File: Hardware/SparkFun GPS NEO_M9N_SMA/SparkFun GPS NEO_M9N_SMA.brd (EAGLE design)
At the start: 40.6 x 33 mm, 89 parts, among them J2 Qwiic Right Angle, J4 Qwiic Right Angle, U1 U-BLOX_NEO-M9N, U2 3.3V, Y1 GPS_CHIP_ANTENNAW3011

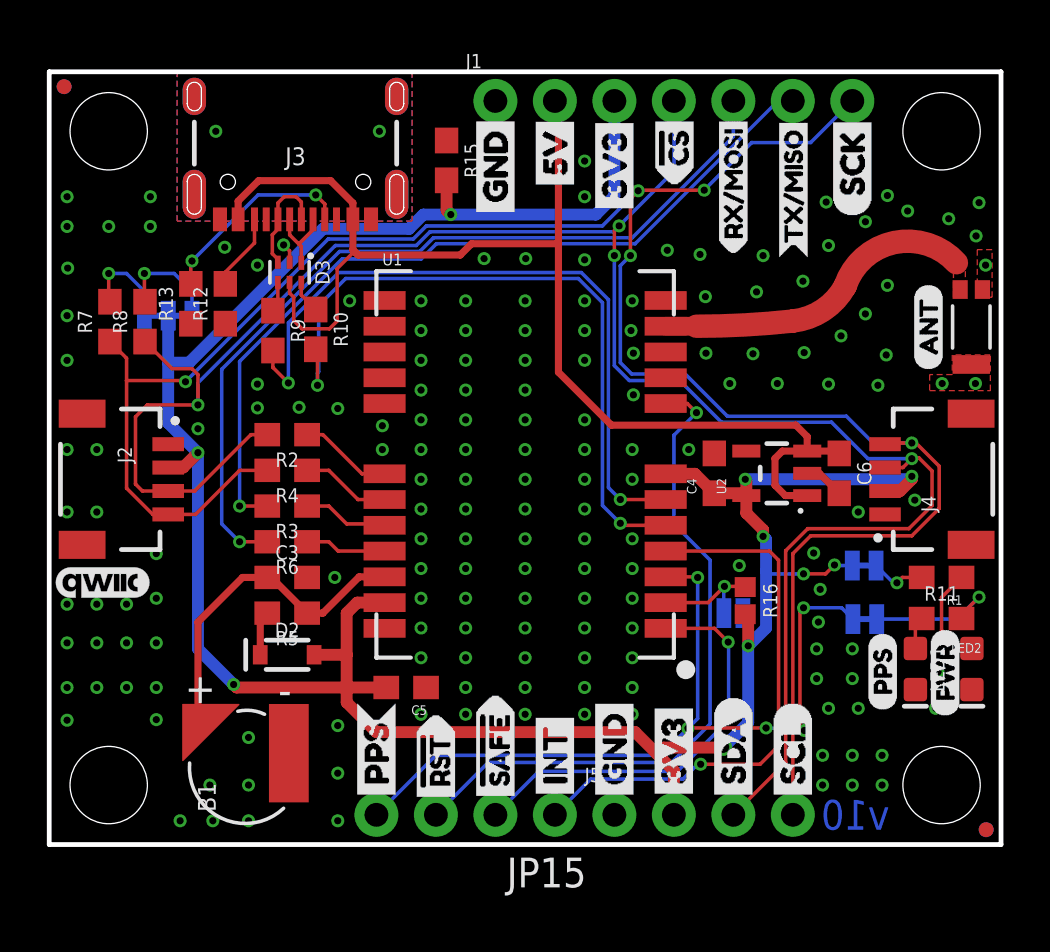
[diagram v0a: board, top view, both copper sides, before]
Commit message: Restore chip antenna version, and moves SMA version to its' own folder
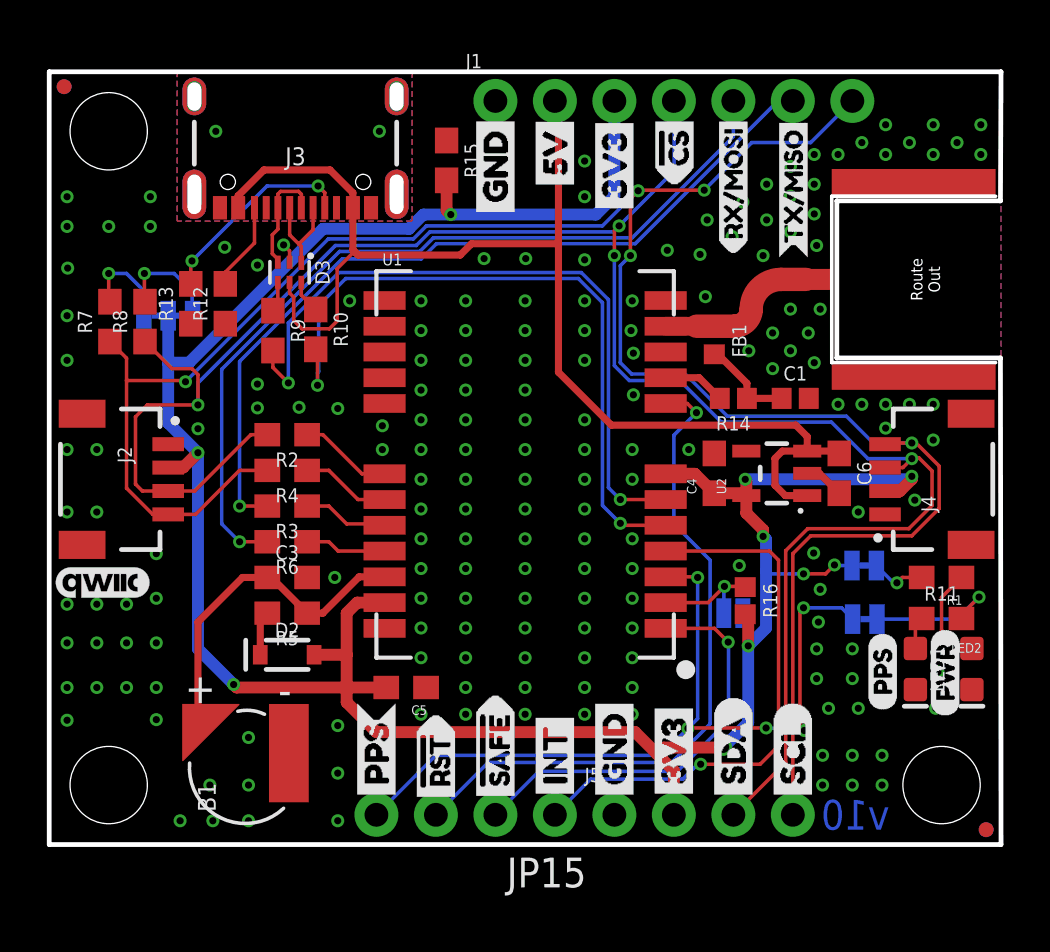
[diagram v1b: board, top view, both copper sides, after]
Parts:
- removed JP41: STAND-OFF, SparkFun:STAND-OFF
- removed U$13: (no value), ANT:ANT0
- removed U$38, U$41: (no value), Labels:SCK-(]-04
- removed Y1: GPS_CHIP_ANTENNAW3011, SparkFun-GPS:W3011
- added C1: 47pF, SparkFun-Capacitors:0402
- added E1: ANTENNA-GROUNDEDEDGE_RPSMA_SMD, SparkFun-RF:SMA-EDGE-SMD
- added FB1: FERRITE_BEAD-120_OHM-0402, SparkFun-Coils:0402
- added R14: 33, SparkFun-Resistors:0402
- J3: device SparkFun-Connectors:USB-C-16P -> SparkFun-Connectors:USB-C-16P-2LAYER-PADS
- U1: device SparkFun-GPS:NEO-M9N -> SparkFun-GPS:NEO-M9N/M8T/M8U
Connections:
- new net N$3: C1.1, FB1.2, R14.1
- net GND: now also C1.2, E1.GND@0, E1.GND@1; no longer Y1.2, Y1.3
- net GPS_ANT1: now also E1.SIG, FB1.1; no longer Y1.1
- net SHLD: no longer J3.SHLD5, J3.SHLD6, J3.SHLD7, J3.SHLD8
- net VCC_RF: now also R14.2
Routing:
- net GPS_ANT1: track 13.0 -> 6.82 mm
- net N$3: track 0.00 -> 4.03 mm
- net VCC_RF: track 0.00 -> 2.67 mm
- net USB_D-: track 3.36 -> 4.35 mm
- net GND: vias 173 -> 186
- removed copper zone on layer 1, net GPS_ANT1
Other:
- outline, holes or cut-outs redrawn

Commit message: Adds Silk to "LONG" SMA version, adds measures
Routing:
- net GND: track 2.56 -> 4.66 mm
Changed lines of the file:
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@@
 <via x="37.7444" y="30.734" extent="1-16" drill="0.3048"/>
 <via x="35.7124" y="30.734" extent="1-16" drill="0.3048"/>
-<wire x1="14.32" y1="23.2306" x2="13.7406" y2="27.1878" width="0" layer="19" extent="1-1"/>
-<wire x1="7.2906" y1="27.1878" x2="7.493" y2="25.5016" width="0" layer="19" extent="1-1"/>
+<wire x1="7.2906" y1="27.1878" x2="7.366" y2="27.1124" width="0.3048" layer="1"/>
+<wire x1="7.366" y1="27.1124" x2="7.366" y2="26.162" width="0.3048" layer="1"/>
+<wire x1="13.7406" y1="27.1878" x2="13.7406" y2="26.1866" width="0.3048" layer="1"/>
+<wire x1="13.7406" y1="26.1866" x2="13.716" y2="26.162" width="0.3048" layer="1"/>
 </signal>
 <signal name="SCL/SCK">
@@
 <polygon width="0.2032" layer="16">
 <vertex x="15.494" y="32.9946"/>
-<vertex x="15.494" y="26.6192"/>
-<vertex x="5.461" y="26.6192"/>
+<vertex x="15.494" y="26.924"/>
+<vertex x="5.461" y="26.924"/>
 <vertex x="5.461" y="32.9946"/>
 </polygon>
 <polygon width="0.2032" layer="1">
 <vertex x="15.494" y="32.9946"/>
-<vertex x="15.494" y="26.6192"/>
-<vertex x="5.461" y="26.6192"/>
+<vertex x="15.494" y="26.9494"/>
+<vertex x="5.461" y="26.9494"/>
 <vertex x="5.461" y="32.9946"/>
 </polygon>
@@
 <wire x1="12.9656" y1="25.3884" x2="13.081" y2="25.273" width="0.3048" layer="1"/>
 <wire x1="13.081" y1="25.273" x2="13.1826" y2="25.1714" width="0.3048" layer="1"/>
-<wire x1="12.9656" y1="25.3884" x2="12.9656" y2="27.1878" width="0.3048" layer="1"/>
+<wire x1="12.9656" y1="25.3884" x2="12.9656" y2="25.908" width="0.3048" layer="1"/>
+<wire x1="12.9656" y1="25.908" x2="12.9656" y2="27.1878" width="0.3048" layer="1"/>
 <wire x1="12.2925" y1="22.3509" x2="12.2925" y2="24.5883" width="0.1524" layer="1"/>
 <wire x1="13.1826" y1="25.1714" x2="17.5514" y2="25.1714" width="0.3048" layer="1"/>
